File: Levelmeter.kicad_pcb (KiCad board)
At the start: 4 copper layers, 90 x 70 mm, 175 parts, among them J1 JST_PH_2.0mm_1x02, J2 USB_C, J3 Header_50mil_2x07, J4 JST_PH_2.0mm_1x03, J5 Header_100mil_1x06, J6 Header_100mil_1x06, J7 Header_100mil_1x06, J8 Header_100mil_1x02, Q1 DMG2305UX-13, Q2 DMG2305UX-13, Q3 FS8205A, Q4 AO3400A, Q5 AO3400A, SW1 PEC11R-4215F-S0024, SW2 PEC11R-4215F-S0024, U1 LP5907MFX-3.3/NOPB, U10 BL24C256A-SFRC, U11 BME280, U12 SN74HC14PWR, U13 LM35, U14 AD9833BRMZ-REEL7, U15 ADS131M04IPWR, U16 AD826, U2 DW01A, U3 LP5907MFX-3.3/NOPB, U4 TP4056, U5 HX4002-MFC, U6 LM27761DSGR, U7 STM32G0B1RET6, U8 RN4871-I/RM128, U9 SN74AHCT244DBR, Y1 Q13FC1350000400, Y2 X50328MSB2GI

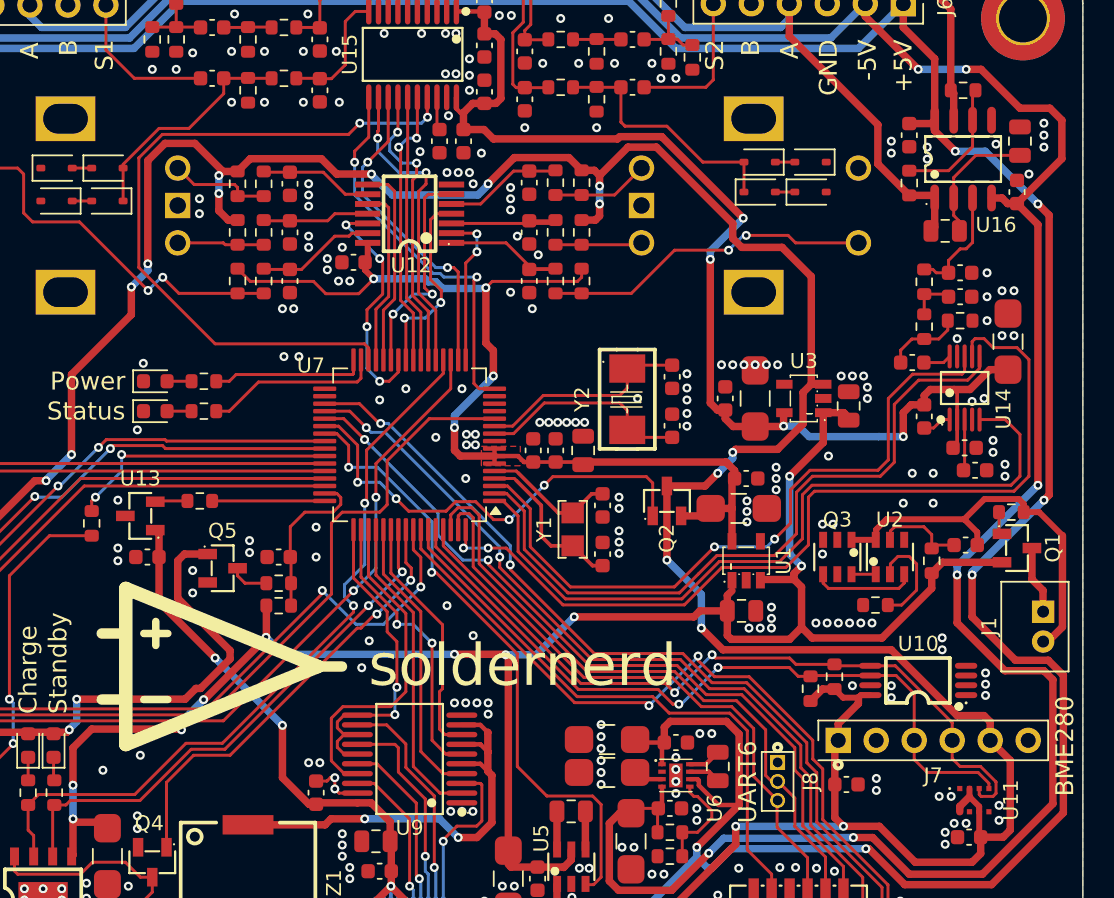
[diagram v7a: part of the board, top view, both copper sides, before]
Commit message: Debug headers for SPI1, SPI2 and SPI3 added
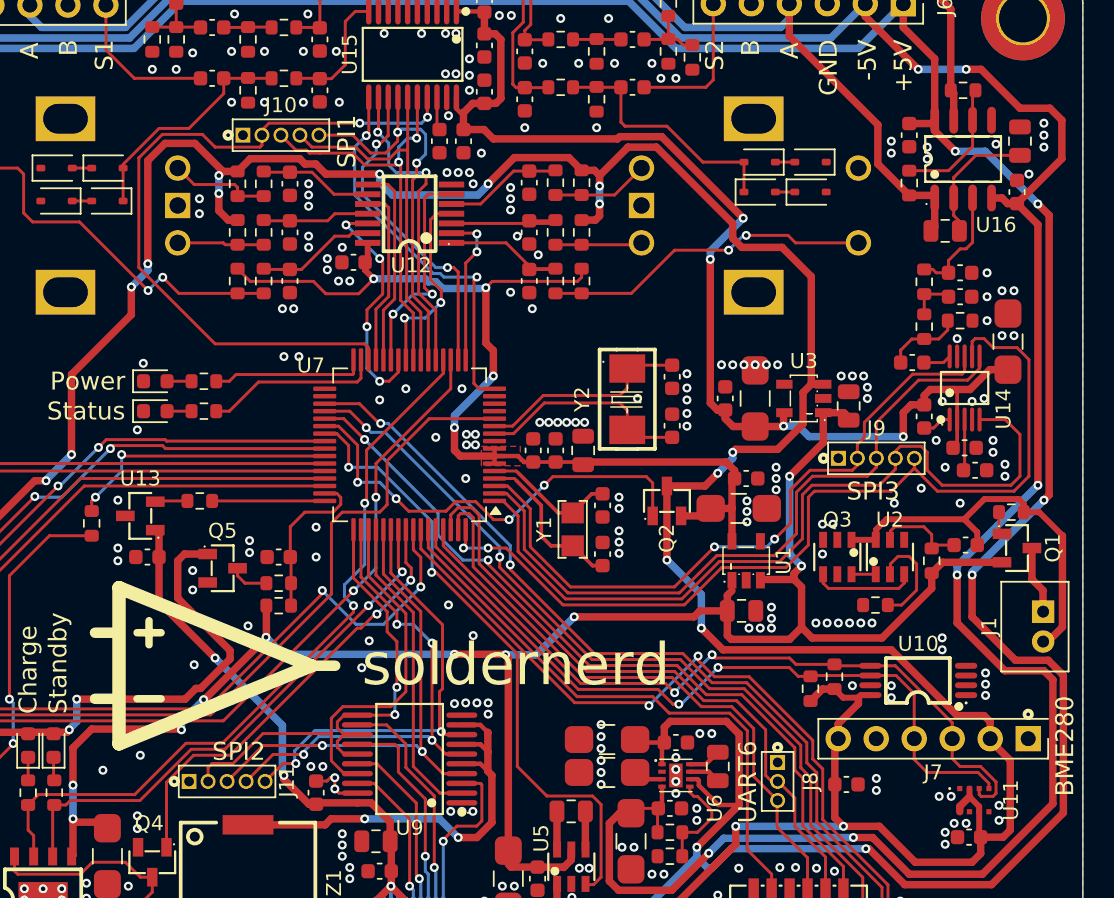
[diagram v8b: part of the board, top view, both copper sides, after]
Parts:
- added J10: Header_50mil_1x05, sldrnrd:Header_50mil_1x05, F.Cu at (86.4, 41.8)
- added J11: Header_50mil_1x05, sldrnrd:Header_50mil_1x05, F.Cu at (82.8, 85.0)
- added J9: Header_50mil_1x05, sldrnrd:Header_50mil_1x05, F.Cu at (126.2, 63.4)
- J8: value Header_100mil_1x02 -> Header_50mil_1x03
- turned J7 to 180 degrees
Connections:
- J7 pad 1: 3V3 -> GND
- J7 pad 2: GND -> 3V3
- J7 pad 3: EEPROM_SCL -> EEPROM_SDA
- J7 pad 4: EEPROM_SDA -> EEPROM_SCL
- J7 pad 5: 3V3 -> GND
- J7 pad 6: GND -> 3V3
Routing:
- net DISP_VCOM: track 19.2 -> 33.7 mm, vias 0 -> 2
- net DISP_CS: track 19.1 -> 33.0 mm, vias 2 -> 4
- net DISP_MOSI: track 16.5 -> 30.3 mm, vias 0 -> 2
- net DISP_SCK: track 22.5 -> 32.6 mm
- net ADC_MOSI: track 18.8 -> 27.6 mm
- net ADC_MISO: track 18.0 -> 26.1 mm
- net ADC_SCK: track 19.7 -> 27.0 mm
- net DAC_Clock: track 50.3 -> 53.8 mm
- net DAC_SCK: track 59.3 -> 61.3 mm
- net ADC_CLOCK: track 47.5 -> 48.8 mm
- net DAC_FSYNC: track 46.5 -> 45.5 mm
- net DAC_MOSI: track 47.6 -> 47.1 mm
- net GND: vias 314 -> 316
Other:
- board text added: "SPI1"
- board text added: "SPI2"
- board text added: "SPI3"
